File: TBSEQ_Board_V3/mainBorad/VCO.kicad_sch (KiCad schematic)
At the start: 30 parts, among them IC11_1 AN6562, IC3 NJM2125F-TE1, J13 Conn_01x01_Pin, Q24 NPN, Q25 NPN, Q26 HN1C01FU-GR,LF, Q27 PNP, Q28 NJFET, Q8 PNP, SW1 2MS1T1B4VS2QES

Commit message: BoardV3
ERCチェック済
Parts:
- removed IC11_1: AN6562, Package_DIP:DIP-8_W7.62mm, symbol Device:Opamp_Dual

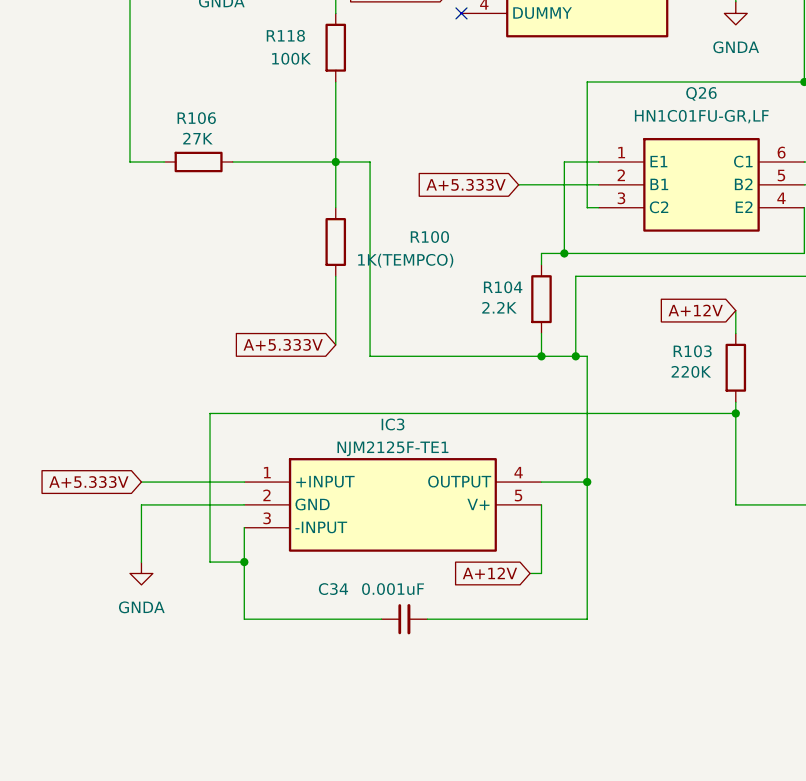
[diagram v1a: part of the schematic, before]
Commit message: V3Board
DualTr フットプリント変更
配線ミス修正
TEMPO削除⇒PanelBoardに移動
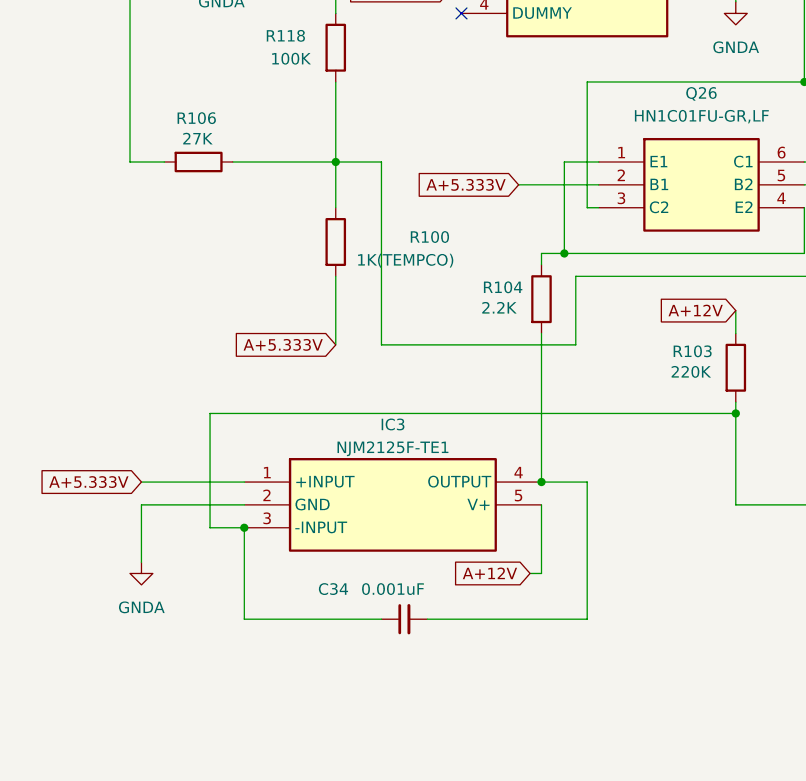
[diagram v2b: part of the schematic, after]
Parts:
- Q26: footprint SamacSys_Parts:HN1C01FUGRLF -> SamacSys_Parts:HN1C01FUGRLF_SOT23&DIP8
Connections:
- net at Q26.5 (B2), R100.1, R106.1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: no longer C34.2, IC3.4 (OUTPUT), R104.2
- new net: C34.2, IC3.4 (OUTPUT), R104.2
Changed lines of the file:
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@@
 	)
 	(junction
-		(at 93.98 118.11)
-		(diameter 0)
-		(color 0 0 0 0)
-	)
-	(junction
 		(at 146.05 87.63)
 		(diameter 0)
@@
 	)
 	(junction
-		(at 72.39 111.76)
+		(at 74.93 100.33)
 		(diameter 0)
 		(color 0 0 0 0)
@@
 	)
 	(junction
-		(at 186.69 106.68)
+		(at 72.39 125.73)
 		(diameter 0)
 		(color 0 0 0 0)
 	)
 	(junction
-		(at 77.47 125.73)
+		(at 186.69 106.68)
 		(diameter 0)
 		(color 0 0 0 0)
@@
 	)
 	(junction
-		(at 74.93 100.33)
-		(diameter 0)
-		(color 0 0 0 0)
-	)
-	(junction
-		(at 76.2 111.76)
+		(at 49.53 90.17)
 		(diameter 0)
 		(color 0 0 0 0)
 	)
 	(junction
-		(at 39.37 134.62)
+		(at 26.67 49.53)
 		(diameter 0)
 		(color 0 0 0 0)
 	)
 	(junction
-		(at 49.53 90.17)
+		(at 237.49 78.74)
 		(diameter 0)
 		(color 0 0 0 0)
 	)
 	(junction
-		(at 26.67 49.53)
+		(at 123.19 45.72)
 		(diameter 0)
 		(color 0 0 0 0)
 	)
 	(junction
-		(at 237.49 78.74)
+		(at 93.98 118.11)
 		(diameter 0)
 		(color 0 0 0 0)
 	)
 	(junction
-		(at 123.19 45.72)
+		(at 176.53 99.06)
 		(diameter 0)
 		(color 0 0 0 0)
 	)
 	(junction
-		(at 176.53 99.06)
+		(at 186.69 82.55)
 		(diameter 0)
 		(color 0 0 0 0)
 	)
 	(junction
-		(at 186.69 82.55)
+		(at 93.98 68.58)
 		(diameter 0)
 		(color 0 0 0 0)
 	)
 	(junction
-		(at 93.98 68.58)
+		(at 39.37 130.81)
 		(diameter 0)
 		(color 0 0 0 0)
@@
 	(wire
 		(pts
-			(xy 39.37 130.81) (xy 39.37 134.62)
-		)
-		(stroke
-			(width 0)
-			(type default)
-		)
-	)
-	(wire
-		(pts
 			(xy 199.39 128.27) (xy 146.05 128.27)
 		)
@@
 	(wire
 		(pts
-			(xy 72.39 111.76) (xy 53.34 111.76)
+			(xy 35.56 130.81) (xy 35.56 118.11)
 		)
 		(stroke
@@
 	(wire
 		(pts
-			(xy 35.56 134.62) (xy 35.56 118.11)
+			(xy 203.2 82.55) (xy 186.69 82.55)
 		)
 		(stroke
@@
 	(wire
 		(pts
-			(xy 203.2 82.55) (xy 186.69 82.55)
+			(xy 110.49 90.17) (xy 110.49 128.27)
 		)
 		(stroke
@@
 	(wire
 		(pts
-			(xy 110.49 90.17) (xy 110.49 128.27)
+			(xy 93.98 68.58) (xy 93.98 66.04)
 		)
 		(stroke
@@
 	(wire
 		(pts
-			(xy 93.98 68.58) (xy 93.98 66.04)
+			(xy 93.98 128.27) (xy 110.49 128.27)
 		)
 		(stroke
@@
 	(wire
 		(pts
-			(xy 93.98 128.27) (xy 110.49 128.27)
+			(xy 49.53 68.58) (xy 49.53 73.66)
 		)
 		(stroke
@@
 	(wire
 		(pts
-			(xy 49.53 68.58) (xy 49.53 73.66)
+			(xy 91.44 68.58) (xy 93.98 68.58)
 		)
 		(stroke
@@
 	(wire
 		(pts
-			(xy 91.44 68.58) (xy 93.98 68.58)
+			(xy 35.56 118.11) (xy 93.98 118.11)
 		)
 		(stroke
@@
 	(wire
 		(pts
-			(xy 227.33 82.55) (xy 232.41 82.55)
+			(xy 72.39 100.33) (xy 72.39 101.6)
 		)
 		(stroke
@@
 	(wire
 		(pts
-			(xy 39.37 134.62) (xy 39.37 140.97)
+			(xy 227.33 82.55) (xy 232.41 82.55)
 		)
 		(stroke
@@
 	(wire
 		(pts
-			(xy 237.49 68.58) (xy 237.49 78.74)
+			(xy 39.37 130.81) (xy 39.37 140.97)
 		)
 		(stroke
@@
 	(wire
 		(pts
-			(xy 77.47 111.76) (xy 76.2 111.76)
+			(xy 237.49 68.58) (xy 237.49 78.74)
 		)
 		(stroke
@@
 	(wire
 		(pts
-			(xy 35.56 118.11) (xy 93.98 118.11)
+			(xy 76.2 110.49) (xy 54.61 110.49)
 		)
 		(stroke
@@
 	(wire
 		(pts
-			(xy 93.98 118.11) (xy 93.98 128.27)
-		)
-		(stroke
-			(width 0)
-			(type default)
-		)
-	)
-	(wire
-		(pts
 			(xy 26.67 90.17) (xy 30.48 90.17)
 		)
@@
 	(wire
 		(pts
-			(xy 72.39 100.33) (xy 72.39 101.6)
+			(xy 237.49 78.74) (xy 240.03 78.74)
 		)
 		(stroke
@@
 	(wire
 		(pts
-			(xy 237.49 78.74) (xy 240.03 78.74)
+			(xy 101.6 81.28) (xy 127 81.28)
 		)
 		(stroke
@@
 	(wire
 		(pts
-			(xy 101.6 81.28) (xy 127 81.28)
+			(xy 186.69 121.92) (xy 186.69 116.84)
 		)
 		(stroke
@@
 	(wire
 		(pts
-			(xy 186.69 121.92) (xy 186.69 116.84)
+			(xy 123.19 35.56) (xy 123.19 36.83)
 		)
 		(stroke
@@
 	(wire
 		(pts
-			(xy 123.19 35.56) (xy 123.19 36.83)
+			(xy 184.15 60.96) (xy 186.69 60.96)
 		)
 		(stroke
@@
 	(wire
 		(pts
-			(xy 184.15 60.96) (xy 186.69 60.96)
+			(xy 72.39 125.73) (xy 77.47 125.73)
 		)
 		(stroke
@@
 	(wire
 		(pts
-			(xy 77.47 125.73) (xy 77.47 111.76)
+			(xy 72.39 100.33) (xy 74.93 100.33)
 		)
 		(stroke
@@
 	(wire
 		(pts
-			(xy 237.49 78.74) (xy 237.49 87.63)
+			(xy 54.61 90.17) (xy 54.61 110.49)
 		)
 		(stroke
@@
 	(wire
 		(pts
-			(xy 111.76 45.72) (xy 123.19 45.72)
+			(xy 237.49 78.74) (xy 237.49 87.63)
 		)
 		(stroke
@@
 	(wire
 		(pts
-			(xy 186.69 106.68) (xy 186.69 109.22)
+			(xy 111.76 45.72) (xy 123.19 45.72)
 		)
 		(stroke
@@
 	(wire
 		(pts
-			(xy 72.39 111.76) (xy 72.39 109.22)
+			(xy 186.69 106.68) (xy 186.69 109.22)
 		)
 		(stroke
@@
 	(wire
 		(pts
+			(xy 72.39 109.22) (xy 72.39 125.73)
+		)
+		(stroke
+			(width 0)
+			(type default)
+		)
+	)
+	(wire
+		(pts
 			(xy 72.39 135.89) (xy 72.39 128.27)
 		)
@@
 	(wire
 		(pts
-			(xy 53.34 90.17) (xy 53.34 111.76)
+			(xy 104.14 102.87) (xy 76.2 102.87)
 		)
 		(stroke
@@
 	(wire
 		(pts
-			(xy 74.93 100.33) (xy 72.39 100.33)
-		)
-		(stroke
-			(width 0)
-			(type default)
-		)
-	)
-	(wire
-		(pts
-			(xy 77.47 125.73) (xy 72.39 125.73)
-		)
-		(stroke
-			(width 0)
-			(type default)
-		)
-	)
-	(wire
-		(pts
 			(xy 78.74 92.71) (xy 69.85 92.71)
 		)
@@
 	(wire
 		(pts
-			(xy 104.14 102.87) (xy 76.2 102.87)
-		)
-		(stroke
-			(width 0)
-			(type default)
-		)
-	)
-	(wire
-		(pts
 			(xy 176.53 87.63) (xy 176.53 99.06)
 		)
@@
 	(wire
 		(pts
-			(xy 123.19 45.72) (xy 123.19 48.26)
+			(xy 76.2 102.87) (xy 76.2 110.49)
 		)
 		(stroke
@@
 	(wire
 		(pts
-			(xy 121.92 148.59) (xy 121.92 154.94)
+			(xy 123.19 45.72) (xy 123.19 48.26)
 		)
 		(stroke
@@
 	(wire
 		(pts
-			(xy 76.2 111.76) (xy 72.39 111.76)
+			(xy 121.92 148.59) (xy 121.92 154.94)
 		)
 		(stroke
@@
 	(wire
 		(pts
-			(xy 39.37 134.62) (xy 35.56 134.62)
+			(xy 39.37 130.81) (xy 35.56 130.81)
 		)
 		(stroke
@@
 	(wire
 		(pts
-			(xy 53.34 90.17) (xy 49.53 90.17)
+			(xy 54.61 90.17) (xy 49.53 90.17)
 		)
 		(stroke
@@
 	(wire
 		(pts
-			(xy 76.2 102.87) (xy 76.2 111.76)
+			(xy 93.98 118.11) (xy 93.98 128.27)
 		)
 		(stroke
@@
 			)
 		)
-		(property "Footprint" "SamacSys_Parts:HN1C01FUGRLF"
+		(property "Footprint" "SamacSys_Parts:HN1C01FUGRLF_SOT23&DIP8"
 			(at 97.79 185.09 0)
 			(effects

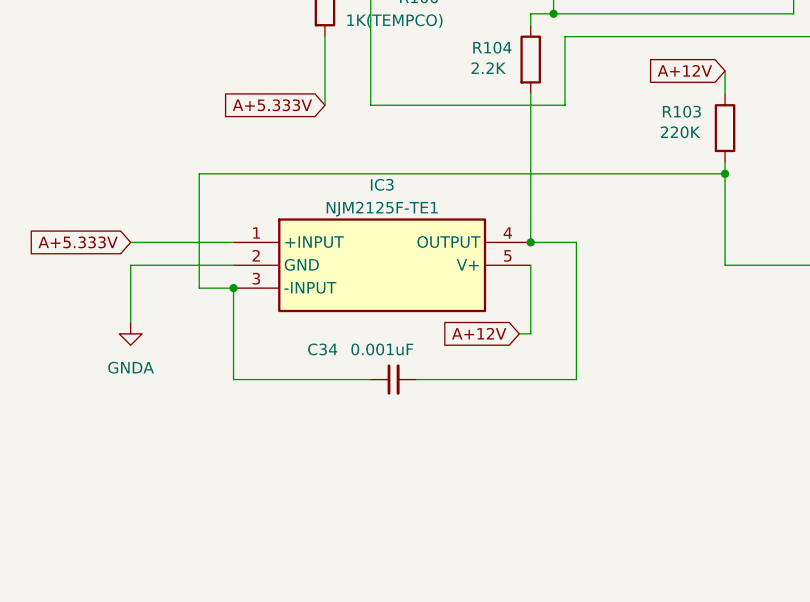
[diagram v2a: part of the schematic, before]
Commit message: V3Board
opamp Dip8に対応
部品配置
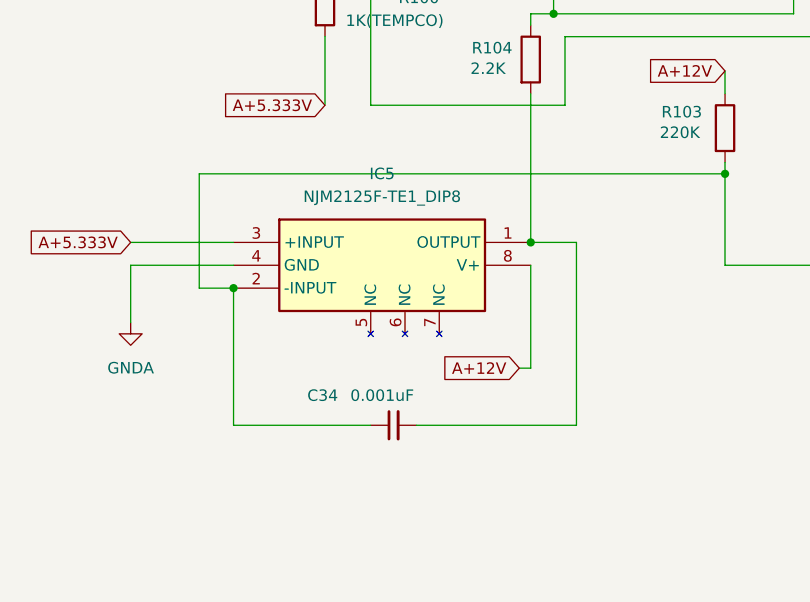
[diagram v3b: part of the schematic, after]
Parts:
- removed IC3: NJM2125F-TE1, SOT95P280X130-5N, symbol SamacSys_Parts:NJM2125F-TE1
- added IC5: NJM2125F-TE1_DIP8, SamacSys_Parts:NJM2125F-SOT95&DIP8, symbol SamacSys_Parts:NJM2125F-TE1_DIP-8
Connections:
- net A+12V: now also IC5.8 (V+)
- net A+5.333V: now also IC5.3 (+INPUT)
- net GNDA: now also IC5.4 (GND)
- net at C34.1, Q26.6 (C1), R102.1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: now also IC5.2 (-INPUT)
- net at C34.2, R104.2: now also IC5.1 (OUTPUT)
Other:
- moved on the sheet: C34

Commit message: V3Board
アートワーク仮配置
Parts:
- Q24, Q25, Q27, Q28, Q8: footprint Package_TO_SOT_THT:TO-92_Inline -> Package_TO_SOT_THT:TO-92_HandSolder
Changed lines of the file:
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@@
 			)
 		)
-		(property "Footprint" "Package_TO_SOT_THT:TO-92_Inline"
+		(property "Footprint" "Package_TO_SOT_THT:TO-92_HandSolder"
 			(at 99.06 50.8 0)
 			(effects
@@
 			)
 		)
-		(property "Footprint" "Package_TO_SOT_THT:TO-92_Inline"
+		(property "Footprint" "Package_TO_SOT_THT:TO-92_HandSolder"
 			(at 125.73 50.8 0)
 			(effects
@@
 			)
 		)
-		(property "Footprint" "Package_TO_SOT_THT:TO-92_Inline"
+		(property "Footprint" "Package_TO_SOT_THT:TO-92_HandSolder"
 			(at 125.73 33.02 0)
 			(effects
@@
 			)
 		)
-		(property "Footprint" "Package_TO_SOT_THT:TO-92_Inline"
+		(property "Footprint" "Package_TO_SOT_THT:TO-92_HandSolder"
 			(at 139.7 78.74 0)
 			(effects
@@
 			)
 		)
-		(property "Footprint" "Package_TO_SOT_THT:TO-92_Inline"
+		(property "Footprint" "Package_TO_SOT_THT:TO-92_HandSolder"
 			(at 189.23 101.6 0)
 			(effects

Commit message: V3Board
GNDパターン塗り済
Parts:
- C11: footprint Capacitor_THT:CP_Radial_D5.0mm_P2.00mm -> Capacitor_THT:CP_Radial_D4.0mm_P2.00mm
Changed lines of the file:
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@@
 			)
 		)
-		(property "Footprint" "Capacitor_THT:CP_Radial_D5.0mm_P2.00mm"
+		(property "Footprint" "Capacitor_THT:CP_Radial_D4.0mm_P2.00mm"
 			(at 203.2 87.63 0)
 			(effects

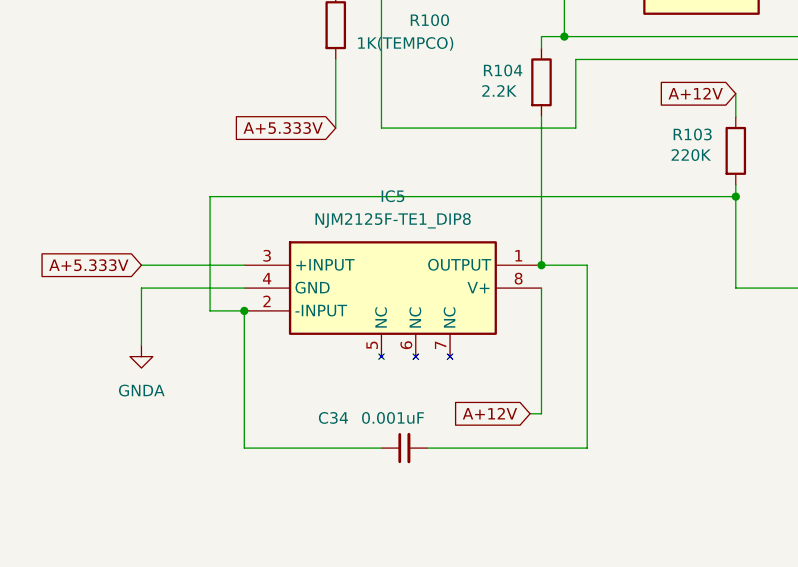
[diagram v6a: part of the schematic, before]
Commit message: V3Board
スペーサー穴追加
オートルーター後
DualTr,OPアンプは表面実装に切り替え
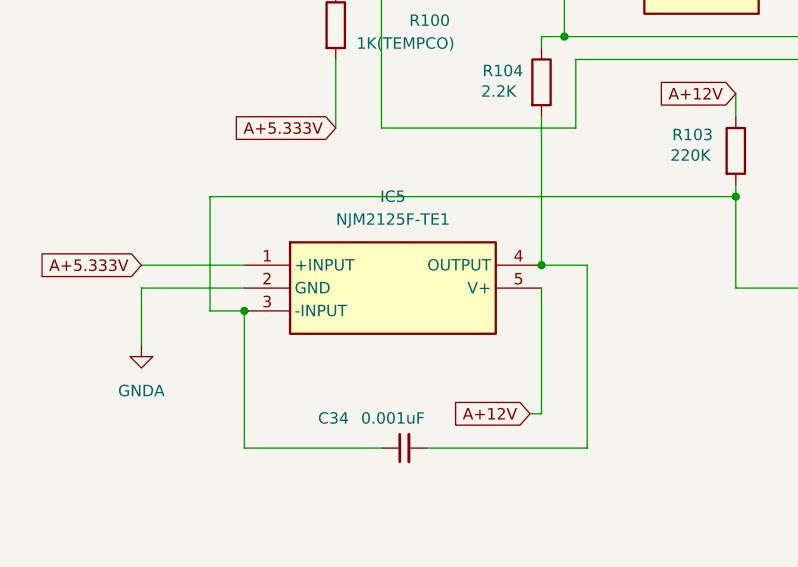
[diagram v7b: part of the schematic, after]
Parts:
- removed IC5: NJM2125F-TE1_DIP8, SamacSys_Parts:NJM2125F-SOT95&DIP8, symbol SamacSys_Parts:NJM2125F-TE1_DIP-8
- added IC5: NJM2125F-TE1, SamacSys_Parts:SOT95P280X130-5N, symbol SamacSys_Parts:NJM2125F-TE1
- Q26: footprint SamacSys_Parts:HN1C01FUGRLF_SOT23&DIP8 -> SamacSys_Parts:HN1C01FUGRLF
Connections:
- net A+12V: now also IC5.5 (V+)
- net A+5.333V: now also IC5.1 (+INPUT)
- net GNDA: now also IC5.2 (GND)
- net at C34.1, Q26.6 (C1), R102.1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: now also IC5.3 (-INPUT)
- net at C34.2, R104.2: now also IC5.4 (OUTPUT)
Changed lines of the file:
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@@
 	)
 	(junction
-		(at 146.05 87.63)
+		(at 72.39 125.73)
 		(diameter 0)
 		(color 0 0 0 0)
 	)
 	(junction
-		(at 72.39 125.73)
+		(at 146.05 87.63)
 		(diameter 0)
 		(color 0 0 0 0)
@@
 	)
 	(junction
-		(at 74.93 100.33)
+		(at 39.37 130.81)
 		(diameter 0)
 		(color 0 0 0 0)
 	)
 	(junction
-		(at 137.16 87.63)
+		(at 74.93 100.33)
 		(diameter 0)
 		(color 0 0 0 0)
 	)
 	(junction
-		(at 39.37 130.81)
+		(at 137.16 87.63)
 		(diameter 0)
 		(color 0 0 0 0)
@@
 	)
 	(symbol
-		(lib_id "SamacSys_Parts:NJM2125F-TE1_DIP-8")
-		(at 39.37 125.73 0)
-		(unit 1)
-		(exclude_from_sim no)
-		(in_bom yes)
-		(on_board yes)
-		(dnp no)
-		(fields_autoplaced yes)
-		(property "Reference" "IC5"
-			(at 55.88 118.11 0)
-			(effects
-				(font
-					(size 1.27 1.27)
-				)
-			)
-		)
-		(property "Value" "NJM2125F-TE1_DIP8"
-			(at 55.88 120.65 0)
-			(effects
-				(font
-					(size 1.27 1.27)
-				)
-			)
-		)
-		(property "Footprint" "SamacSys_Parts:NJM2125F-SOT95&DIP8"
-			(at 68.58 220.65 0)
-			(effects
-				(font
-					(size 1.27 1.27)
-				)
-				(justify left top)
-				(hide yes)
-			)
-		)
-		(property "Datasheet" "https://componentsearchengine.com/Datasheets/1/NJM2125F-TE1.pdf"
-			(at 68.58 320.65 0)
-			(effects
-				(font
-					(size 1.27 1.27)
-				)
-				(justify left top)
-				(hide yes)
-			)
-		)
-		(property "Description" "Operational Amplifiers - Op Amps Single Supply"
-			(at 39.37 125.73 0)
-			(effects
-				(font
-					(size 1.27 1.27)
-				)
-				(hide yes)
-			)
-		)
-		(property "Height" "1.3"
-			(at 68.58 520.65 0)
-			(effects
-				(font
-					(size 1.27 1.27)
-				)
-				(justify left top)
-				(hide yes)
-			)
-		)
-		(property "Manufacturer_Name" "New Japan Radio"
-			(at 68.58 620.65 0)
-			(effects
-				(font
-					(size 1.27 1.27)
-				)
-				(justify left top)
-				(hide yes)
-			)
-		)
-		(property "Manufacturer_Part_Number" "NJM2125F-TE1"
-			(at 68.58 720.65 0)
-			(effects
-				(font
-					(size 1.27 1.27)
-				)
-				(justify left top)
-				(hide yes)
-			)
-		)
-		(property "Mouser Part Number" "513-NJM2125F-TE1"
-			(at 68.58 820.65 0)
-			(effects
-				(font
-					(size 1.27 1.27)
-				)
-				(justify left top)
-				(hide yes)
-			)
-		)
-		(property "Mouser Price/Stock" "https://www.mouser.co.uk/ProductDetail/NJR/NJM2125F-TE1?qs=SzzEZJ0VecQ3YU3q3zUUYw%3D%3D"
-			(at 68.58 920.65 0)
-			(effects
-				(font
-					(size 1.27 1.27)
-				)
-				(justify left top)
-				(hide yes)
-			)
-		)
-		(property "Arrow Part Number" ""
-			(at 68.58 1020.65 0)
-			(effects
-				(font
-					(size 1.27 1.27)
-				)
-				(justify left top)
-				(hide yes)
-			)
-		)
-		(property "Arrow Price/Stock" ""
-			(at 68.58 1120.65 0)
-			(effects
-				(font
-					(size 1.27 1.27)
-				)
-				(justify left top)
-				(hide yes)
-			)
-		)
-		(property "Sim.Library" ""
-			(at 39.37 125.73 0)
-			(effects
-				(font
-					(size 1.27 1.27)
-				)
-				(hide yes)
-			)
-		)
-		(property "Sim.Name" ""
-			(at 39.37 125.73 0)
-			(effects
-				(font
-					(size 1.27 1.27)
-				)
-				(hide yes)
-			)
-		)
-		(pin "8"
-		)
-		(pin "2"
-		)
-		(pin "3"
-		)
-		(pin "5"
-		)
-		(pin "4"
-		)
-		(pin "6"
-		)
-		(pin "1"
-		)
-		(pin "7"
-		)
-		(instances
-			(project ""
-				(path "/83af791a-9776-40a7-82ad-9528ff7474b8/765da965-e62c-424b-9b1b-9538054aabf6"
-					(reference "IC5")
-					(unit 1)
-				)
-			)
-		)
-	)
-	(symbol
 		(lib_id "Device:Q_NPN_ECB")
 		(at 104.14 53.34 0)
@@
 	)
 	(symbol
+		(lib_id "SamacSys_Parts:NJM2125F-TE1")
+		(at 39.37 125.73 0)
+		(unit 1)
+		(exclude_from_sim no)
+		(in_bom yes)
+		(on_board yes)
+		(dnp no)
+		(fields_autoplaced yes)
+		(property "Reference" "IC5"
+			(at 55.88 118.11 0)
+			(effects
+				(font
+					(size 1.27 1.27)
+				)
+			)
+		)
+		(property "Value" "NJM2125F-TE1"
+			(at 55.88 120.65 0)
+			(effects
+				(font
+					(size 1.27 1.27)
+				)
+			)
+		)
+		(property "Footprint" "SamacSys_Parts:SOT95P280X130-5N"
+			(at 68.58 220.65 0)
+			(effects
+				(font
+					(size 1.27 1.27)
+				)
+				(justify left top)
+				(hide yes)
+			)
+		)
+		(property "Datasheet" "https://componentsearchengine.com/Datasheets/1/NJM2125F-TE1.pdf"
+			(at 68.58 320.65 0)
+			(effects
+				(font
+					(size 1.27 1.27)
+				)
+				(justify left top)
+				(hide yes)
+			)
+		)
+		(property "Description" "Operational Amplifiers - Op Amps Single Supply"
+			(at 39.37 125.73 0)
+			(effects
+				(font
+					(size 1.27 1.27)
+				)
+				(hide yes)
+			)
+		)
+		(property "Height" "1.3"
+			(at 68.58 520.65 0)
+			(effects
+				(font
+					(size 1.27 1.27)
+				)
+				(justify left top)
+				(hide yes)
+			)
+		)
+		(property "Manufacturer_Name" "New Japan Radio"
+			(at 68.58 620.65 0)
+			(effects
+				(font
+					(size 1.27 1.27)
+				)
+				(justify left top)
+				(hide yes)
+			)
+		)
+		(property "Manufacturer_Part_Number" "NJM2125F-TE1"
+			(at 68.58 720.65 0)
+			(effects
+				(font
+					(size 1.27 1.27)
+				)
+				(justify left top)
+				(hide yes)
+			)
+		)
+		(property "Mouser Part Number" "513-NJM2125F-TE1"
+			(at 68.58 820.65 0)
+			(effects
+				(font
+					(size 1.27 1.27)
+				)
+				(justify left top)
+				(hide yes)
+			)
+		)
+		(property "Mouser Price/Stock" "https://www.mouser.co.uk/ProductDetail/NJR/NJM2125F-TE1?qs=SzzEZJ0VecQ3YU3q3zUUYw%3D%3D"
+			(at 68.58 920.65 0)
+			(effects
+				(font
+					(size 1.27 1.27)
+				)
+				(justify left top)
+				(hide yes)
+			)
+		)
+		(property "Arrow Part Number" ""
+			(at 68.58 1020.65 0)
+			(effects
+				(font
+					(size 1.27 1.27)
+				)
+				(justify left top)
+				(hide yes)
+			)
+		)
+		(property "Arrow Price/Stock" ""
+			(at 68.58 1120.65 0)
+			(effects
+				(font
+					(size 1.27 1.27)
+				)
+				(justify left top)
+				(hide yes)
+			)
+		)
+		(pin "1"
+		)
+		(pin "4"
+		)
+		(pin "3"
+		)
+		(pin "2"
+		)
+		(pin "5"
+		)
+		(instances
+			(project ""
+				(path "/83af791a-9776-40a7-82ad-9528ff7474b8/765da965-e62c-424b-9b1b-9538054aabf6"
+					(reference "IC5")
+					(unit 1)
+				)
+			)
+		)
+	)
+	(symbol
 		(lib_id "Device:R")
 		(at 49.53 77.47 0)
@@
 			)
 		)
-		(property "Footprint" "SamacSys_Parts:HN1C01FUGRLF_SOT23&DIP8"
+		(property "Footprint" "SamacSys_Parts:HN1C01FUGRLF"
 			(at 97.79 185.09 0)
 			(effects
